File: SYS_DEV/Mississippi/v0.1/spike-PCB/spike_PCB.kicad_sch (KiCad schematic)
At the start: 6 parts, among them J1 Power_Input_Screw_Terminal, J2 Sensing_Spike_Screw_Terminal

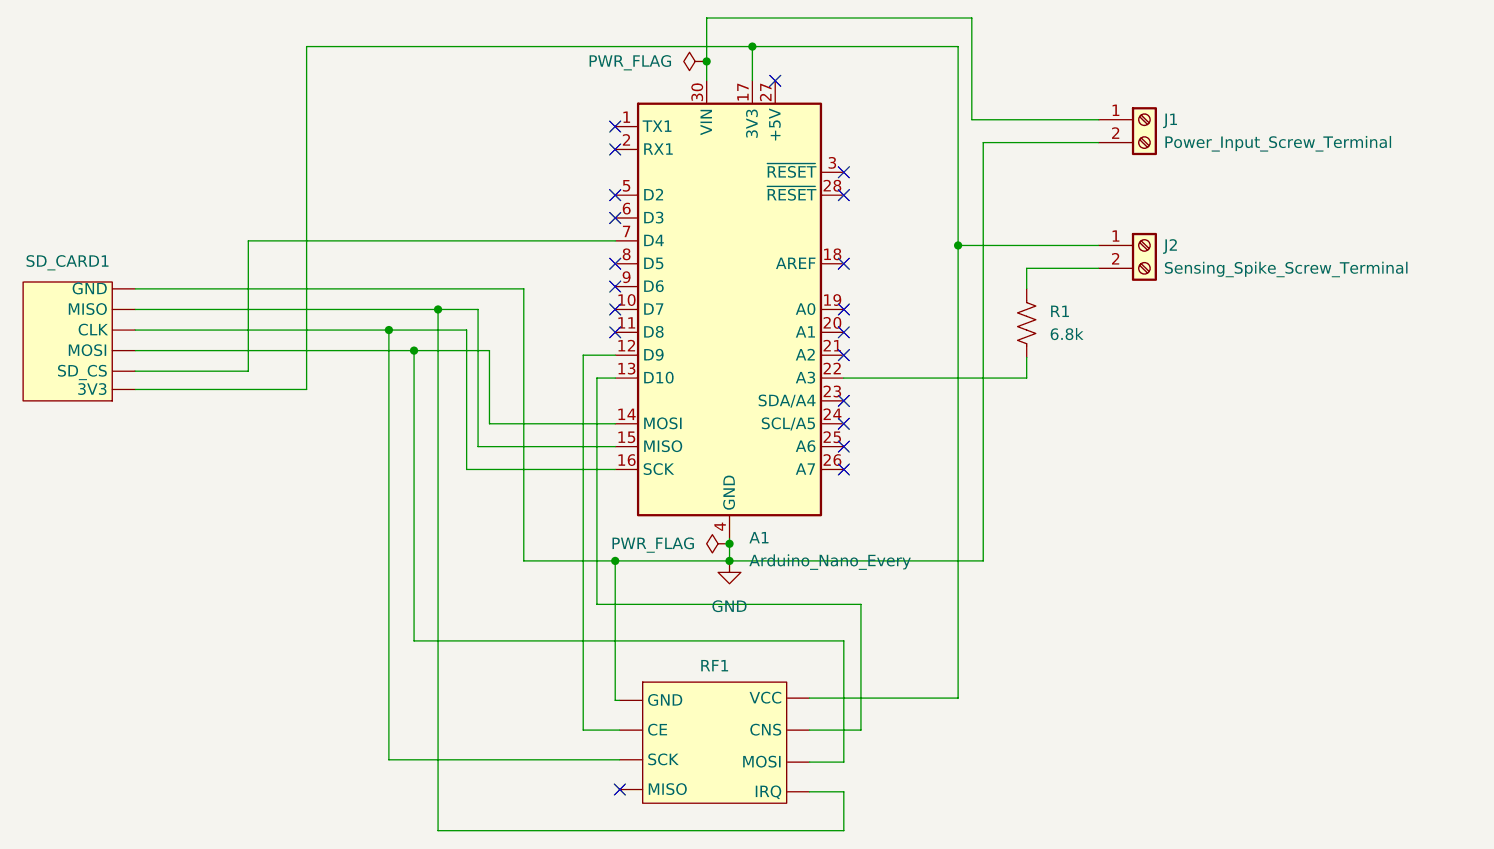
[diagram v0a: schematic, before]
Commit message: updated two errors on PCB
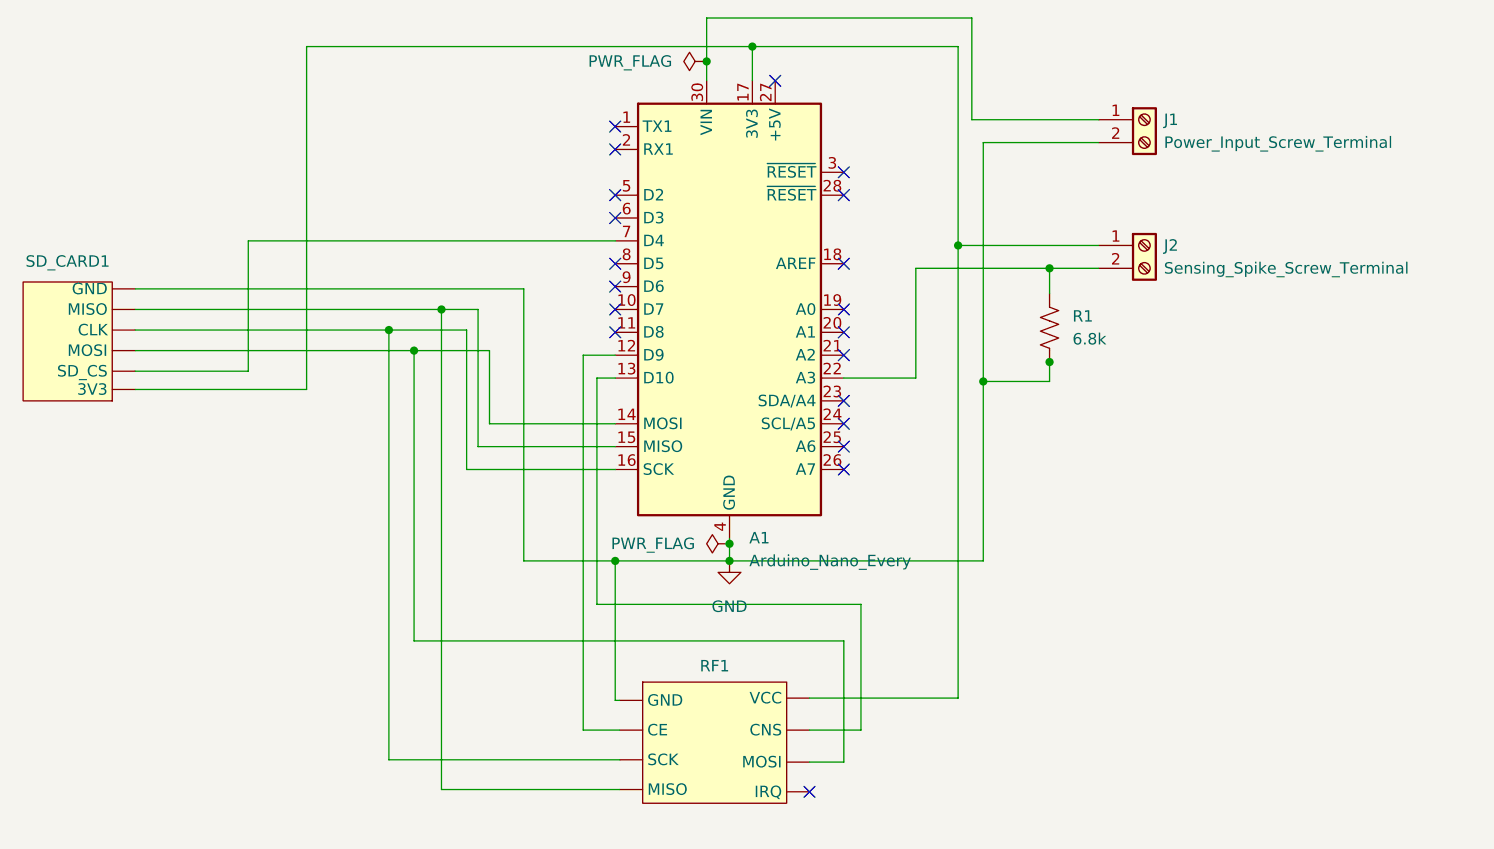
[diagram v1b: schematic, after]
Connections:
- net GND: now also R1.2
- net at J2.2 (Pin_2), R1.1: now also A1.22 (A3)
- net at A1.15 (MISO), SD_CARD1.5 (MISO): now also RF1.4 (MISO); no longer RF1.8 (IRQ)
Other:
- moved on the sheet: R1
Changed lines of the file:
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@@
     (rev "0")
   )
+  (junction (at 203.2 118.872) (diameter 0) (color 0 0 0 0)
+  )
   (junction (at 167.64 140.97) (diameter 0) (color 0 0 0 0)
   )
+  (junction (at 135.636 113.03) (diameter 0) (color 0 0 0 0)
+  )
+  (junction (at 195.834 121.031) (diameter 0) (color 0 0 0 0)
+  )
   (junction (at 154.94 140.97) (diameter 0) (color 0 0 0 0)
   )
@@
   (junction (at 129.794 115.316) (diameter 0) (color 0 0 0 0)
   )
+  (junction (at 203.2 108.458) (diameter 0) (color 0 0 0 0)
+  )
   (junction (at 193.04 105.918) (diameter 0) (color 0 0 0 0)
   )
@@
   )
   (junction (at 165.1 85.471) (diameter 0) (color 0 0 0 0)
-  )
-  (junction (at 135.255 113.03) (diameter 0) (color 0 0 0 0)
   )
   (no_connect (at 180.34 123.19))
@@
   (no_connect (at 154.94 92.71))
   (no_connect (at 154.94 95.25))
-  (no_connect (at 155.448 166.37))
   (no_connect (at 154.94 102.87))
   (no_connect (at 154.94 107.95))
@@
   (no_connect (at 154.94 113.03))
   (no_connect (at 180.34 125.73))
+  (no_connect (at 176.53 166.624))
   (no_connect (at 180.34 130.81))
   (no_connect (at 180.34 100.33))
@@
     (stroke (width 0) (type default))
   )
+  (wire (pts (xy 203.2 118.745) (xy 203.2 118.872))
+    (stroke (width 0) (type default))
+  )
+  (wire (pts (xy 155.448 166.37) (xy 135.636 166.37))
+    (stroke (width 0) (type default))
+  )
   (wire (pts (xy 101.6 115.316) (xy 129.794 115.316))
     (stroke (width 0) (type default))
   )
-  (wire (pts (xy 101.6 113.03) (xy 135.255 113.03))
-    (stroke (width 0) (type default))
-  )
   (wire (pts (xy 101.6 117.602) (xy 132.588 117.602))
     (stroke (width 0) (type default))
@@
     (stroke (width 0) (type default))
   )
+  (wire (pts (xy 188.341 120.65) (xy 180.34 120.65))
+    (stroke (width 0) (type default))
+  )
   (wire (pts (xy 129.794 163.068) (xy 155.448 163.068))
     (stroke (width 0) (type default))
@@
     (stroke (width 0) (type default))
   )
-  (wire (pts (xy 200.66 108.458) (xy 200.66 110.744))
+  (wire (pts (xy 203.2 108.458) (xy 203.2 111.252))
     (stroke (width 0) (type default))
   )
@@
     (stroke (width 0) (type default))
   )
-  (wire (pts (xy 200.66 118.364) (xy 200.66 120.65))
-    (stroke (width 0) (type default))
-  )
-  (wire (pts (xy 208.661 108.458) (xy 200.66 108.458))
+  (wire (pts (xy 203.2 118.872) (xy 203.2 121.031))
+    (stroke (width 0) (type default))
+  )
+  (wire (pts (xy 135.636 113.03) (xy 139.7 113.03))
+    (stroke (width 0) (type default))
+  )
+  (wire (pts (xy 208.661 108.458) (xy 203.2 108.458))
+    (stroke (width 0) (type default))
+  )
+  (wire (pts (xy 195.834 121.031) (xy 195.834 140.97))
     (stroke (width 0) (type default))
   )
@@
     (stroke (width 0) (type default))
   )
-  (wire (pts (xy 176.53 166.624) (xy 180.34 166.624))
-    (stroke (width 0) (type default))
-  )
   (wire (pts (xy 139.7 113.03) (xy 139.7 128.27))
     (stroke (width 0) (type default))
@@
     (stroke (width 0) (type default))
   )
-  (wire (pts (xy 195.834 94.488) (xy 195.834 140.97))
+  (wire (pts (xy 195.834 94.488) (xy 195.834 121.031))
     (stroke (width 0) (type default))
   )
@@
     (stroke (width 0) (type default))
   )
+  (wire (pts (xy 203.2 121.031) (xy 195.834 121.031))
+    (stroke (width 0) (type default))
+  )
   (wire (pts (xy 120.65 83.82) (xy 170.18 83.82))
     (stroke (width 0) (type default))
@@
     (stroke (width 0) (type default))
   )
-  (wire (pts (xy 180.34 166.624) (xy 180.34 170.942))
-    (stroke (width 0) (type default))
-  )
   (wire (pts (xy 144.78 140.97) (xy 154.94 140.97))
     (stroke (width 0) (type default))
   )
-  (wire (pts (xy 135.255 113.03) (xy 139.7 113.03))
+  (wire (pts (xy 101.6 113.03) (xy 135.636 113.03))
     (stroke (width 0) (type default))
   )
@@
     (stroke (width 0) (type default))
   )
+  (wire (pts (xy 203.2 108.458) (xy 188.341 108.458))
+    (stroke (width 0) (type default))
+  )
+  (wire (pts (xy 188.341 108.458) (xy 188.341 120.65))
+    (stroke (width 0) (type default))
+  )
+  (wire (pts (xy 135.636 166.37) (xy 135.636 113.03))
+    (stroke (width 0) (type default))
+  )
   (wire (pts (xy 182.245 159.766) (xy 182.245 145.796))
     (stroke (width 0) (type default))
   )
-  (wire (pts (xy 200.66 120.65) (xy 180.34 120.65))
-    (stroke (width 0) (type default))
-  )
   (wire (pts (xy 144.78 110.744) (xy 144.78 140.97))
     (stroke (width 0) (type default))
@@
     (stroke (width 0) (type default))
   )
-  (wire (pts (xy 180.34 170.942) (xy 135.255 170.942))
-    (stroke (width 0) (type default))
-  )
   (wire (pts (xy 139.7 128.27) (xy 154.94 128.27))
-    (stroke (width 0) (type default))
-  )
-  (wire (pts (xy 135.255 170.942) (xy 135.255 113.03))
     (stroke (width 0) (type default))
   )
@@
     )
   )
-  (symbol (lib_id "Device:R_US") (at 200.66 114.554 0) (unit 1)
+  (symbol (lib_id "Device:R_US") (at 203.2 115.062 0) (unit 1)
     (in_bom yes) (on_board yes) (dnp no) (fields_autoplaced)
-    (property "Reference" "R1" (at 203.2 113.284 0)
+    (property "Reference" "R1" (at 205.74 113.792 0)
       (effects (font (size 1.27 1.27)) (justify left))
     )
-    (property "Value" "6.8k" (at 203.2 115.824 0)
+    (property "Value" "6.8k" (at 205.74 116.332 0)
       (effects (font (size 1.27 1.27)) (justify left))
     )
-    (property "Footprint" "Resistor_THT:R_Axial_DIN0207_L6.3mm_D2.5mm_P7.62mm_Horizontal" (at 201.676 114.808 90)
-      (effects (font (size 1.27 1.27)) hide)
-    )
-    (property "Datasheet" "~" (at 200.66 114.554 0)
-      (effects (font (size 1.27 1.27)) hide)
-    )
+    (property "Footprint" "Resistor_THT:R_Axial_DIN0207_L6.3mm_D2.5mm_P7.62mm_Horizontal" (at 204.216 115.316 90)
+      (effects (font (size 1.27 1.27)) hide)
+    )
+    (property "Datasheet" "~" (at 203.2 115.062 0)
+      (effects (font (size 1.27 1.27)) hide)
+    )
